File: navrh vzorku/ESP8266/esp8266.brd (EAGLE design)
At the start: 160 x 100 mm, 23 parts

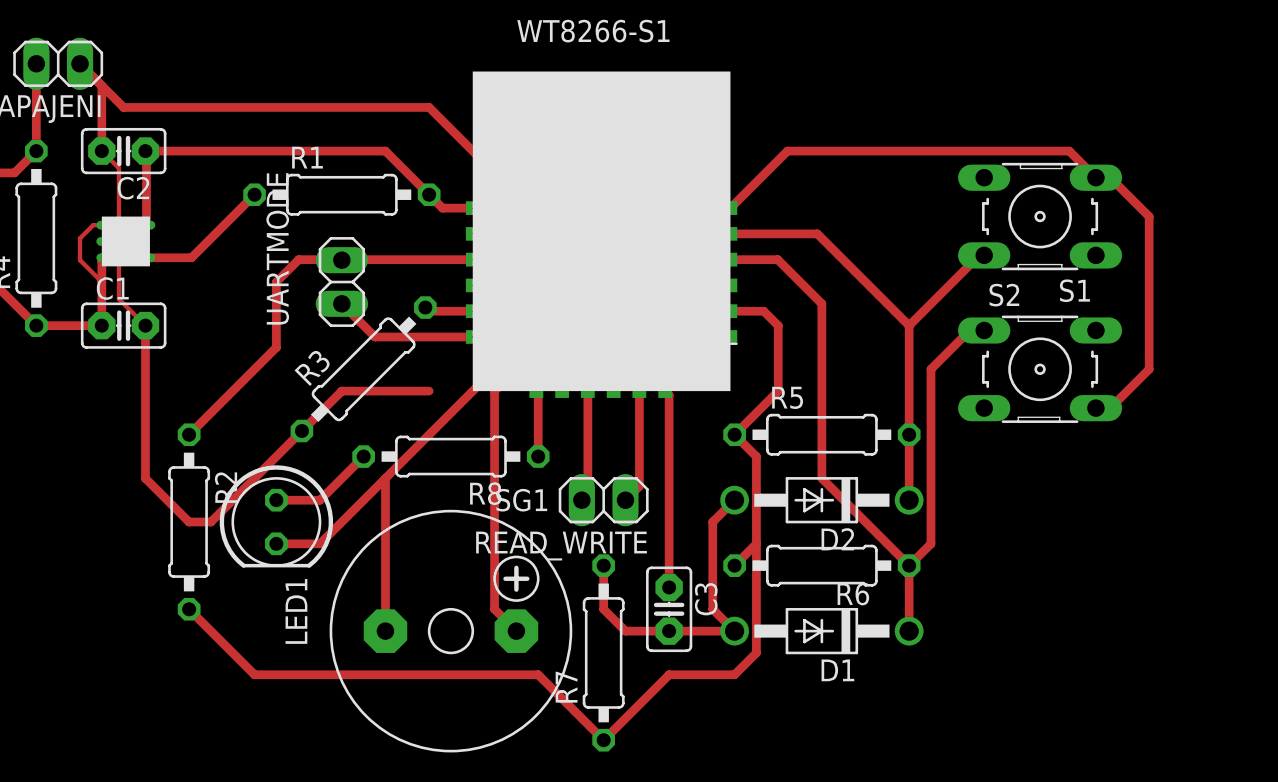
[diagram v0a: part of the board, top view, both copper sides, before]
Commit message: Dokumetace tvorba esp8266 vzorku
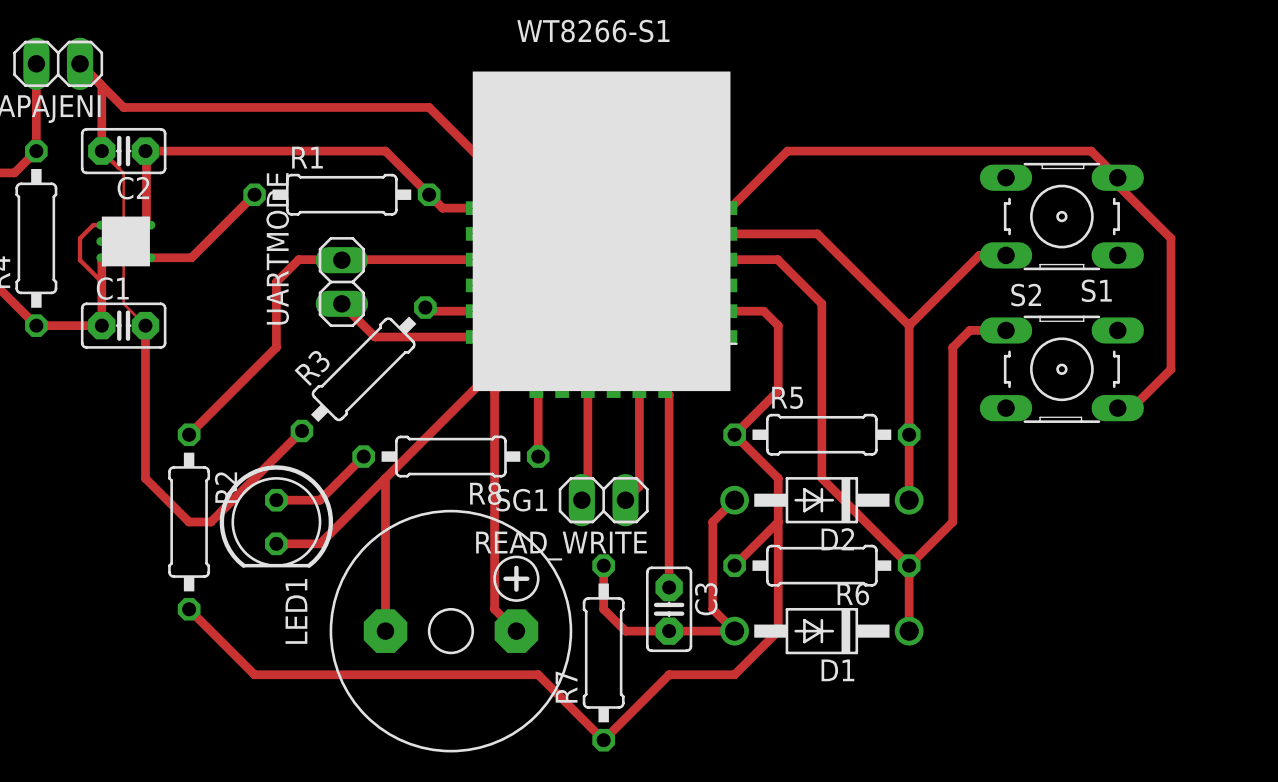
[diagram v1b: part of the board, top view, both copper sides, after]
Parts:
- moved S1 1.27 mm to (77.5, 36.8)
- moved S2 1.27 mm to (77.5, 27.9)
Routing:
- net N$6: track 128.9 -> 121.6 mm
- net N$2: track 106.1 -> 108.9 mm
- net N$13: track 28.8 -> 30.1 mm
- net N$12: track 43.5 -> 44.8 mm

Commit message: Plosne spoje
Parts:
- moved LED1 9.16 mm to (24.1, 14.0)
- moved R2 8.98 mm to (17.8, 17.8)
- moved MERENI_UBYTKU_NAPETI 8.89 mm to (5.08, 38.1)
- moved R4 6.35 mm to (11.4, 35.6)
- moved R7 5.68 mm to (45.7, 8.89)
- moved C3 5.24 mm to (49.5, 12.7)
- moved READ_WRITE 5.24 mm to (45.7, 19.1)
- moved SG1 5.24 mm to (36.8, 11.4)
- moved U$1 5.24 mm to (38.1, 27.9)
- moved R1 5.08 mm to (30.5, 38.1)
- moved UARTMODE 5.08 mm to (30.5, 33.0)
- moved NAPAJENI 5.08 mm to (14.0, 45.7)
- moved C1 5.08 mm to (17.8, 30.5)
- moved C2 5.08 mm to (17.8, 40.6)
- moved D1 5.08 mm to (58.4, 12.7)
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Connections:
- removed net N$18: LED1.K, SG1.-, U$1.GND2
- removed net N$6: C1.2, C2.2, NAPAJENI.1, R3.1, S1.3, S2.4, U$1.GND, U$2.GND
- new net GND: C1.2, C2.2, LED1.K, NAPAJENI.1, R3.1, S1.3, S2.4, SG1.-, U$1.GND, U$1.GND2, U$2.GND
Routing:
- net GND: track 0.00 -> 180.4 mm
- net N$6: track 121.6 -> 0.00 mm
- net N$18: track 35.8 -> 0.00 mm
- net N$1: track 20.6 -> 31.1 mm
- net N$2: track 108.9 -> 118.7 mm
- net N$16: track 6.13 -> 10.8 mm
- net N$3: track 23.0 -> 26.4 mm
- net N$10: track 9.42 -> 12.5 mm
- net N$11: track 11.5 -> 14.1 mm
- net N$5: track 6.49 -> 9.03 mm
- net N$7: track 6.69 -> 9.23 mm
- net N$17: track 21.2 -> 18.7 mm
- net N$15: track 3.86 -> 5.13 mm
- net N$8: track 8.42 -> 9.49 mm
- net N$9: track 2.85 -> 3.50 mm
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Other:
- board size 160 x 100 mm -> 83.8 x 51.7 mm
- board text added: "ESP8266"
- board text added: "Milan Jiricek"

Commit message: Finalni verze
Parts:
- removed MERENI_UBYTKU_NAPETI: (no value), pinhead:1X02
- removed R4: 10, rcl:0207/10
- added JP1, JP2: (no value), pinhead:1X03
- added Q1, Q2: IRF4905, transistor-power:TO220BH
- added R10, R9: 2k, rcl:0207/10
- R2, R5, R6, R7: value 10k -> 2k
- moved R2 45.0 mm to (34.3, 59.7), turned to 90 degrees
- moved R5 42.2 mm to (73.7, 63.5), turned to 270 degrees
- moved R7 28.5 mm to (35.6, 35.6), turned to 0 degrees
- moved D2 24.5 mm to (67.3, 43.2)
- moved NAPAJENI 24.1 mm to (14.0, 69.8)
- moved C2 23.0 mm to (15.2, 63.5), turned to 0 degrees
- moved U$2 21.6 mm to (15.2, 58.4)
- moved R6 20.8 mm to (71.1, 33.0), turned to 90 degrees
- moved R1 20.5 mm to (22.9, 57.1), turned to 90 degrees
- moved READ_WRITE 20.5 mm to (25.4, 21.6), turned to 90 degrees
- moved C3 19.4 mm to (53.3, 31.8)
- moved S1 18.0 mm to (69.8, 19.1), turned to 90 degrees
- moved D1 17.8 mm to (58.4, 30.5), turned to 90 degrees
- moved C1 16.7 mm to (15.2, 47.0)
- moved UARTMODE 14.5 mm to (34.3, 47.0)
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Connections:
- removed net N$10: MERENI_UBYTKU_NAPETI.1, NAPAJENI.2, R4.2
- removed net N$8: U$1.GND1, UARTMODE.1
- new net N$18: JP1.3, Q1.D, Q2.D, R9.1, U$1.IO16
- new net N$19: JP1.2, U$1.EN
- new net N$20: JP1.1, R10.2
- new net N$6: C2.1, JP2.1, Q1.S, Q2.S, R1.2, R10.1, R2.2, R5.1, R6.1, R7.1, U$1.3.3V, U$2.OUT
- net GND: now also R9.2, S2.3, U$1.GND1, UARTMODE.1
- net N$1: now also JP2.3; no longer MERENI_UBYTKU_NAPETI.2, R4.1
- net N$12: now also Q2.G
- net N$13: now also Q1.G
- net N$2: now also JP2.2, NAPAJENI.2; no longer C2.1, R1.2, R2.2, R5.1, R6.1, R7.1, U$1.3.3V, U$1.EN, U$2.OUT
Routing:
- net N$6: track 0.00 -> 232.3 mm
- net N$18: track 0.00 -> 141.3 mm, vias 0 -> 3
- net N$2: track 118.7 -> 18.9 mm
- net N$13: track 30.6 -> 95.5 mm
- net N$7: track 9.23 -> 71.9 mm
- net N$5: track 9.03 -> 63.0 mm
- net N$12: track 45.3 -> 73.8 mm
- net N$19: track 0.00 -> 24.1 mm, vias 0 -> 1
- net N$15: track 5.13 -> 20.8 mm
- net N$9: track 3.50 -> 18.5 mm
- net N$10: track 12.5 -> 0.00 mm
- net N$14: track 18.9 -> 31.2 mm
- net N$3: track 26.4 -> 14.5 mm
- net N$20: track 0.00 -> 10.2 mm
- net N$1: track 31.1 -> 21.5 mm
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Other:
- board size 83.8 x 51.7 mm -> 119.4 x 78.4 mm
- board text added: "NETIO CONTROLLER PROTOTYPE"
